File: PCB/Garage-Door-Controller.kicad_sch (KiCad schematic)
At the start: 0 parts

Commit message: Started schematic with most components
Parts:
- added C1, C2, C3, C4, C5, C6, C9: C, symbol Device:C
- added C10, C11: 22pF, symbol Device:C
- added C7: 0u1F, symbol Device:C
- added C8: 10uF, symbol Device:C
- added D1: 1N5819HW-7-F, symbol Device:D_Zener
- added D5, D6, D7: LESD5D5.0CT1G, symbol Device:D_TVS_Filled
- added J1: USB_C_Receptacle_USB2.0_16P, symbol Connector:USB_C_Receptacle_USB2.0_16P
- added J2: Conn_02x08_Counter_Clockwise, Connector_PinHeader_2.54mm:PinHeader_2x08_P2.54mm_Vertical, symbol Connector_Generic:Conn_02x08_Counter_Clockwise
- added R1, R2: 5k1, symbol Device:R_US
- added R3, R4, R5, R6: R_US, symbol Device:R_US
- added R7, R8: 10k, symbol Device:R_US
- added SW1, SW2: SW_Push_Dual, symbol Switch:SW_Push_Dual
- added U1: ESP32-C3-MINI-1, PCM_Espressif:ESP32-C3-MINI-1, symbol PCM_Espressif:ESP32-C3-MINI-1
- added U2: AMS1117-3.3, Package_TO_SOT_SMD:SOT-223-3_TabPin2, symbol Regulator_Linear:AMS1117-3.3
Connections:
- new net: J2.1 (Pin_1), U1.12 (GPIO0/ADC1_CH0/XTAL_32K_P)
- new net: J2.10 (Pin_10), U1.23 (GPIO9)
- new net: J2.11 (Pin_11), U1.16 (GPIO10)
- new net: J2.12 (Pin_12), U1.30 (GPIO20/U0RXD)
- new net: J2.13 (Pin_13), U1.31 (GPIO21/U0TXD)
- new net: J2.2 (Pin_2), U1.13 (GPIO1/ADC1_CH1/XTAL_32K_N)
- new net: J2.3 (Pin_3), R8.1, U1.5 (GPIO2/ADC1_CH2)
- new net: J2.4 (Pin_4), U1.6 (GPIO3/ADC1_CH3)
- new net: J2.5 (Pin_5), U1.18 (GPIO4/ADC1_CH4)
- new net: J2.6 (Pin_6), U1.19 (GPIO5/ADC2_CH0)
- new net: J2.7 (Pin_7), U1.20 (GPIO6)
- new net: J2.8 (Pin_8), U1.21 (GPIO7)
- new net: J2.9 (Pin_9), R6.1, U1.22 (GPIO8)
- new net: D1.2 (A), D5.2 (A2), J1.A4 (VBUS), J1.A9 (VBUS), J1.B4 (VBUS), J1.B9 (VBUS)
- new net: J1.B5 (CC2), R2.2
- new net: J1.A5 (CC1), R1.2
- new net CHIP_PU: C9.1, R7.1
- new net D +: C10.1, D7.2 (A2), J1.A6 (D+), J1.B6 (D+)
- new net D -: C11.1, D6.2 (A2), J1.A7 (D-), J1.B7 (D-)
- new net ESP_3V3: R7.2
- new net GND: C10.2, C11.2, C7.1, C8.1, D5.1 (A1), D6.1 (A1), D7.1 (A1), J1.A1 (GND), J1.A12 (GND), J1.B1 (GND), J1.B12 (GND), J1.SH (SHIELD), J2.16 (Pin_16), R1.1, R2.1, U1.1 (GND), U1.11 (GND), U1.14 (GND), U1.2 (GND), U1.36 (GND), U1.37 (GND), U1.38 (GND), U1.39 (GND), U1.40 (GND), U1.41 (GND), U1.42 (GND), U1.43 (GND), U1.44 (GND), U1.45 (GND), U1.46 (GND), U1.47 (GND), U1.48 (GND), U1.49 (GND), U1.50 (GND), U1.51 (GND), U1.52 (GND), U1.53 (GND)
- new net VCC_3V3: C7.2, C8.2, J2.15 (Pin_15), R6.2, R8.2, U1.3 (3V3)
- new net VCC_5V: D1.1 (K), J2.14 (Pin_14)
- no-connect marks 0 -> 2
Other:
- note added: "ESP32-C3-MINI-1"
- note added: "USB-C"

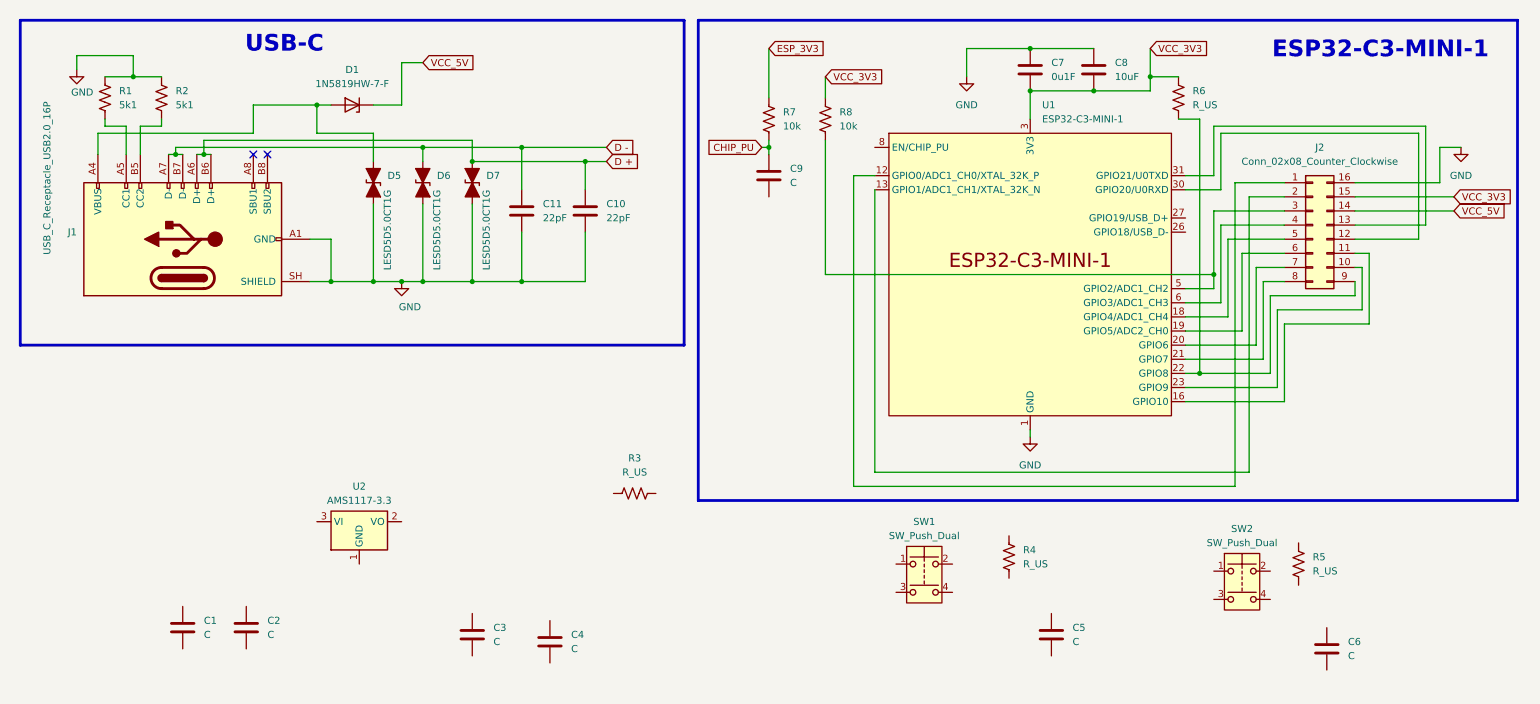
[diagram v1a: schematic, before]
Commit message: Finished basic wiring and added most footprints
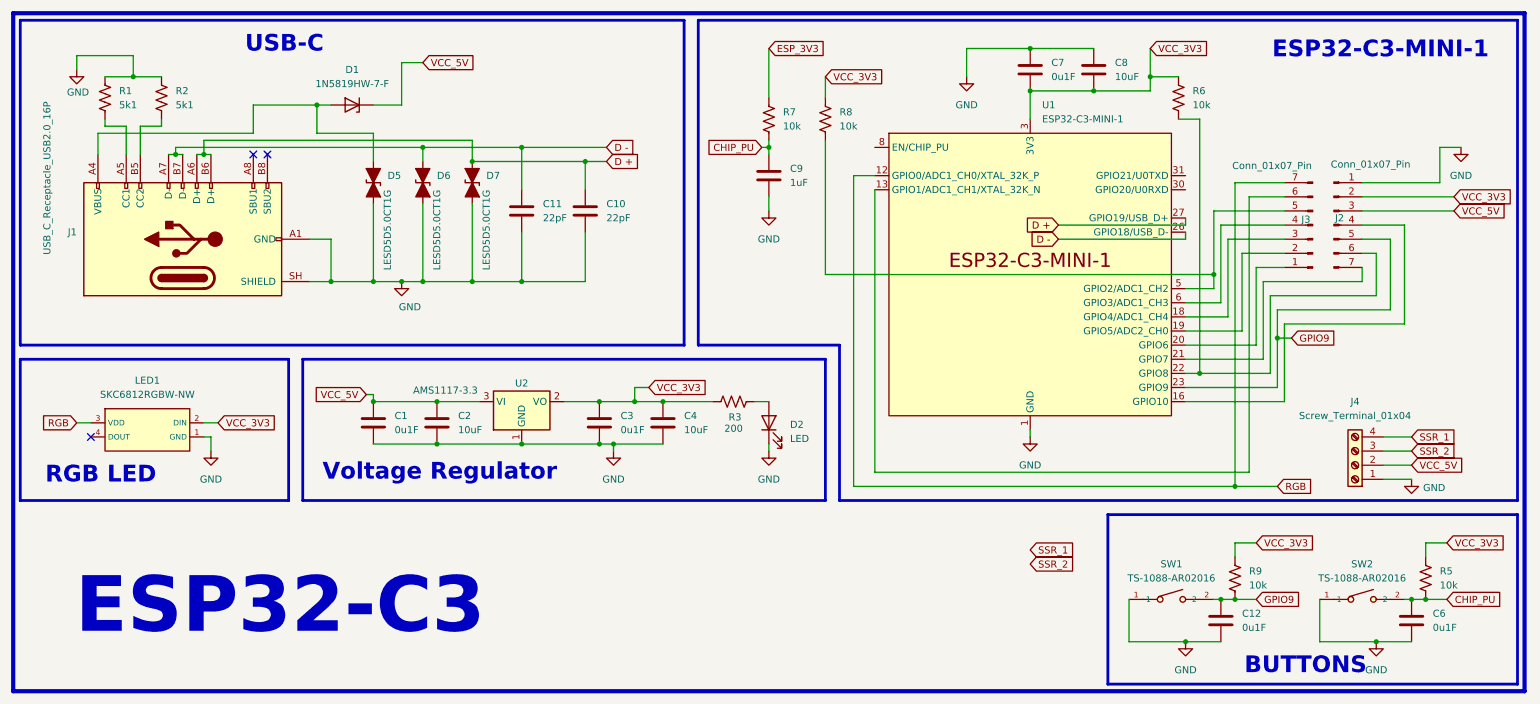
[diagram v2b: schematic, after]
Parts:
- removed C5: C, symbol Device:C
- removed J2: Conn_02x08_Counter_Clockwise, Connector_PinHeader_2.54mm:PinHeader_2x08_P2.54mm_Vertical, symbol Connector_Generic:Conn_02x08_Counter_Clockwise
- removed R4: R_US, symbol Device:R_US
- removed SW1, SW2: SW_Push_Dual, symbol Switch:SW_Push_Dual
- added C12: 0u1F, Capacitor_SMD:C_0603_1608Metric, symbol Device:C
- added D2: LED, LED_SMD:LED_0603_1608Metric, symbol Device:LED
- added J2, J3: Conn_01x07_Pin, Connector_PinSocket_2.54mm:PinSocket_1x07_P2.54mm_Vertical, symbol Connector:Conn_01x07_Pin
- added J4: Screw_Terminal_01x04, symbol Connector:Screw_Terminal_01x04
- added LED1: SKC6812RGBW-NW, lcsc_footprints:C5348912_LED-SMD_4P-L5_0-W4_9-BR, symbol lcsc_imported:SKC6812RGBW-NW
- added R9: 10k, Resistor_SMD:R_0603_1608Metric, symbol Device:R_US
- added SW1, SW2: TS-1088-AR02016, lcsc_footprints:C720477_SW-SMD_L3_9-W3_0-P4_45, symbol lcsc_imported:TS-1088-AR02016
- C1, C3, C6: value C -> 0u1F; footprint (none) -> Capacitor_SMD:C_0603_1608Metric
- C10, C11, C7: footprint (none) -> Capacitor_SMD:C_0603_1608Metric
- C2, C4: value C -> 10uF; footprint (none) -> Capacitor_SMD:C_0805_2012Metric
- C8: footprint (none) -> Capacitor_SMD:C_0805_2012Metric
- C9: value C -> 1uF; footprint (none) -> Capacitor_SMD:C_0603_1608Metric
- D1: footprint (none) -> Diode_SMD:D_SOD-123
- D5, D6, D7: footprint (none) -> Diode_SMD:D_SOD-523
- J1: footprint (none) -> lcsc_footprints:C53436595_USB-TYPE-C-SMD_JS16T-TYPE-C057-H730
- R1, R2: footprint (none) -> Resistor_SMD:R_0805_2012Metric
- R3: value R_US -> 200; footprint (none) -> Resistor_SMD:R_0805_2012Metric
- R5, R6: value R_US -> 10k; footprint (none) -> Resistor_SMD:R_0603_1608Metric
- R7, R8: footprint (none) -> Resistor_SMD:R_0603_1608Metric
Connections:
- net CHIP_PU: now also C6.1, R5.1, SW2.2
- net D +: now also U1.27 (GPIO19/USB_D+)
- net D -: now also U1.26 (GPIO18/USB_D-)
- net GND: now also C1.2, C2.2, C3.2, C4.2, C6.2, C9.2, U2.1 (GND), C12.2, D2.1 (K), J2.1 (Pin_1), J4.1 (Pin_1), LED1.1 (GND), SW1.1, SW2.1
- net VCC_3V3: now also C3.1, C4.1, R3.1, R5.2, U2.2 (VO), J2.2 (Pin_2), LED1.2 (DIN), R9.2
- net VCC_5V: now also C1.1, C2.1, U2.3 (VI), J2.3 (Pin_3), J4.2 (Pin_2)
- net at R3.2: now also D2.2 (A)
- net RGB: now reaches U1.12 (GPIO0/ADC1_CH0/XTAL_32K_P)
- net RGB: now also J3.7 (Pin_7), LED1.3 (VDD)
- net GPIO9: now reaches U1.23 (GPIO9)
- net GPIO9: now also C12.1, J2.5 (Pin_5), R9.1, SW1.2
- net at U1.16 (GPIO10): now also J2.4 (Pin_4)
- net at U1.13 (GPIO1/ADC1_CH1/XTAL_32K_N): now also J3.6 (Pin_6)
- net at R8.1, U1.5 (GPIO2/ADC1_CH2): now also J3.5 (Pin_5)
- net at U1.6 (GPIO3/ADC1_CH3): now also J3.4 (Pin_4)
- net at U1.18 (GPIO4/ADC1_CH4): now also J3.3 (Pin_3)
- net at U1.19 (GPIO5/ADC2_CH0): now also J3.2 (Pin_2)
- net at U1.20 (GPIO6): now also J3.1 (Pin_1)
- net at U1.21 (GPIO7): now also J2.7 (Pin_7)
- net at R6.1, U1.22 (GPIO8): now also J2.6 (Pin_6)
- new net SSR_1: J4.4 (Pin_4)
- new net SSR_2: J4.3 (Pin_3)
- no-connect marks 2 -> 3
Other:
- note added: "BUTTONS"
- note added: "ESP32-C3"
- note added: "RGB LED"
- note added: "Voltage Regulator"
- moved on the sheet: C1, C2, C3, C4, C6, R3, R5, U2

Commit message: Finish basic schematic
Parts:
- added R4: 150, Resistor_SMD:R_0805_2012Metric, symbol Device:R_US
- added U3: LTV-817S-TA1-C, lcsc_footprints:C109227_OPTO-SMD-4_L4_6-W6_5-P2_54-LS10_3-BL, symbol lcsc_imported:LTV-817S-TA1-C
- J2, J3: now left out of the parts list
- J4: footprint (none) -> TerminalBlock_Phoenix:TerminalBlock_Phoenix_MKDS-1,5-4-5.08_1x04_P5.08mm_Horizontal
- R3: value 200 -> 150
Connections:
- net GND: now also U3.2
- net OPTO_IN: now reaches J3.6 (Pin_6), U1.13 (GPIO1/ADC1_CH1/XTAL_32K_N)
- net OPTO_IN: now also R4.1
- new net: R4.2, U3.1
- new net OPTO_1: U3.4
- new net OPTO_2: U3.3
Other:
- note added: "Optocoupler"

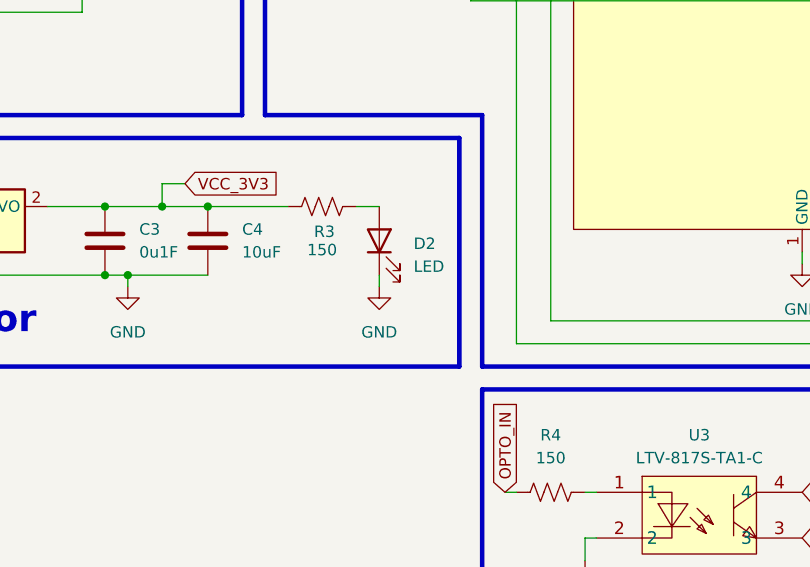
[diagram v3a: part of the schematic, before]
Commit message: Update schematic LED with jlcpcb version
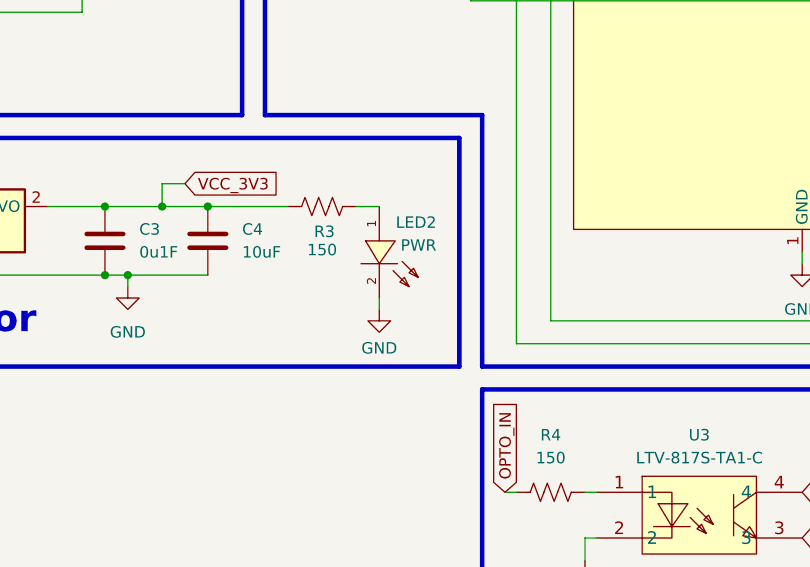
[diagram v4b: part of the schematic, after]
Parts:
- removed D2: LED, LED_SMD:LED_0603_1608Metric, symbol Device:LED
- added LED2: PWR, lcsc_footprints:C2286_LED-SMD_L1_6-W0_8-R-RD, symbol lcsc_imported:0603
- J2, J3: footprint Connector_PinSocket_2.54mm:PinSocket_1x07_P2.54mm_Vertical -> Connector_PinHeader_2.54mm:PinHeader_1x07_P2.54mm_Vertical
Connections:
- net GND: now also LED2.2 (K)
- net at R3.2: now also LED2.1 (A)
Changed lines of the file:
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@@
 	(wire
 		(pts
-			(xy 148.59 91.44) (xy 148.59 90.17)
-		)
-		(stroke
-			(width 0)
-			(type default)
-		)
-	)
-	(wire
-		(pts
 			(xy 148.59 45.72) (xy 148.59 48.26)
 		)
@@
 	(wire
 		(pts
+			(xy 148.59 93.98) (xy 148.59 92.71)
+		)
+		(stroke
+			(width 0)
+			(type default)
+		)
+	)
+	(wire
+		(pts
 			(xy 269.24 36.83) (xy 273.05 36.83)
 		)
@@
 			)
 		)
-		(property "Footprint" "Connector_PinSocket_2.54mm:PinSocket_1x07_P2.54mm_Vertical"
+		(property "Footprint" "Connector_PinHeader_2.54mm:PinHeader_1x07_P2.54mm_Vertical"
 			(at 250.19 50.8 0)
 			(hide yes)
@@
 	(symbol
 		(lib_id "power:GND")
-		(at 148.59 91.44 0)
+		(at 148.59 93.98 0)
 		(unit 1)
 		(body_style 1)
@@
 		(in_pos_files yes)
 		(dnp no)
-		(fields_autoplaced yes)
 		(property "Reference" "#PWR07"
-			(at 148.59 97.79 0)
+			(at 148.59 100.33 0)
 			(hide yes)
 			(show_name no)
@@
 		)
 		(property "Value" "GND"
-			(at 148.59 96.52 0)
+			(at 148.59 98.298 0)
 			(show_name no)
 			(do_not_autoplace no)
@@
 		)
 		(property "Footprint" ""
-			(at 148.59 91.44 0)
+			(at 148.59 93.98 0)
 			(hide yes)
 			(show_name no)
@@
 		)
 		(property "Datasheet" ""
-			(at 148.59 91.44 0)
+			(at 148.59 93.98 0)
 			(hide yes)
 			(show_name no)
@@
 		)
 		(property "Description" "Power symbol creates a global label with name \"GND\" , ground"
-			(at 148.59 91.44 0)
+			(at 148.59 93.98 0)
 			(hide yes)
 			(show_name no)
@@
 			)
 		)
-		(property "Footprint" "Connector_PinSocket_2.54mm:PinSocket_1x07_P2.54mm_Vertical"
+		(property "Footprint" "Connector_PinHeader_2.54mm:PinHeader_1x07_P2.54mm_Vertical"
 			(at 246.38 50.8 0)
 			(hide yes)
@@
 	)
 	(symbol
-		(lib_id "Device:LED")
-		(at 148.59 86.36 90)
+		(lib_id "lcsc_imported:0603")
+		(at 148.59 87.63 270)
+		(mirror x)
 		(unit 1)
 		(body_style 1)
@@
 		(in_pos_files yes)
 		(dnp no)
-		(fields_autoplaced yes)
-		(property "Reference" "D2"
-			(at 152.4 86.6774 90)
+		(property "Reference" "LED2"
+			(at 154.94 84.328 90)
 			(show_name no)
 			(do_not_autoplace no)
@@
 			)
 		)
-		(property "Value" "LED"
-			(at 152.4 89.2174 90)
+		(property "Value" "PWR"
+			(at 154.94 86.868 90)
 			(show_name no)
 			(do_not_autoplace no)
@@
 			)
 		)
-		(property "Footprint" "LED_SMD:LED_0603_1608Metric"
-			(at 148.59 86.36 0)
+		(property "Footprint" "lcsc_footprints:C2286_LED-SMD_L1_6-W0_8-R-RD"
+			(at 138.43 87.63 0)
 			(hide yes)
 			(show_name no)
@@
 			)
 		)
-		(property "Datasheet" ""
-			(at 148.59 86.36 0)
+		(property "Datasheet" "https://www.lcsc.com/datasheet/lcsc_datasheet_1810231112_Hubei-KENTO-Elec-KT-0603R_C2286.pdf"
+			(at 148.717 89.916 0)
+			(hide yes)
+			(show_name no)
+			(do_not_autoplace no)
+			(effects
+				(font
+					(size 1.27 1.27)
+				)
+			)
+		)
+		(property "Description" "0603"
+			(at 148.59 87.63 0)
 			(hide yes)
 			(show_name no)
@@
 			)
 		)
-		(property "Description" "Light emitting diode"
-			(at 148.59 86.36 0)
+		(property "LCSC" "C2286"
+			(at 148.59 87.63 0)
 			(hide yes)
 			(show_name no)
@@
 			)
 		)
-		(property "Sim.Pins" "1=K 2=A"
-			(at 148.59 86.36 0)
+		(property "Manufacturer" "KENTO"
+			(at 148.59 87.63 0)
 			(hide yes)
 			(show_name no)
@@
 			(project "Garage-Door-Controller"
 				(path "/8b0ce9a6-853b-4e12-ac4b-f9d95766b3f3"
-					(reference "D2")
+					(reference "LED2")
 					(unit 1)
 				)
